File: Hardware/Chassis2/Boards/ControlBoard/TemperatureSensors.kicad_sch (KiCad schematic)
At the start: 4 parts, among them J5 TBP02R2W-381-08BE

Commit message: update hw revision 7
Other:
- company: (none) -> Corzine Lab, University of California, Santa Cruz
- title: (none) -> Open Inverter Platform - Control Board
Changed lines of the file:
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@@
 	(generator "eeschema")
 	(generator_version "10.0")
-	(paper "A4")
+	(paper "USLetter")
+	(title_block
+		(title "Open Inverter Platform - Control Board")
+		(date "2026-07-07")
+		(rev "G")
+		(company "Corzine Lab, University of California, Santa Cruz")
+		(comment 1 "Prepared by Thomas Liao")
+	)
 	(junction
 		(at 44.45 40.64)

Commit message: eod 2026-07-08
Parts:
- removed J5: TBP02R2W-381-08BE, TBP02R2W38108BE, symbol InverterCom:TBP02R2W-381-08BE
- removed R13, R29, R30: 10k, Resistor_SMD:R_1210_3225Metric_Pad1.30x2.65mm_HandSolder, symbol Device:R
- added C208, C209, C210, C211: 10uF, Capacitor_SMD:C_1210_3225Metric_Pad1.33x2.70mm_HandSolder, symbol Device:C
- added J1, J4, J5: B2B-XH-AM_LF__SN_, InverterCom:B2BXHAMLFSN, symbol InverterCom:B2B-XH-AM_LF__SN_
- added R90, R92, R94, R96: 10k, Resistor_SMD:R_1210_3225Metric_Pad1.30x2.65mm_HandSolder, symbol Device:R
- added R91, R93, R95, R97: 1k, Resistor_SMD:R_1210_3225Metric_Pad1.30x2.65mm_HandSolder, symbol Device:R
- added Z5, Z6, Z7, Z8: MM3Z3V0ST1G, InverterCom:SOD2512X100N, symbol InverterCom:MM3Z3V0ST1G
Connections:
- net +3.3V_V: now also R90.2, R92.2, R94.2, R96.2
- net GND_V: now also C208.2, C209.2, C210.2, C211.2, J1.1, J4.1, J5.1, Z5.2 (A), Z6.2 (A), Z7.2 (A), Z8.2 (A)
- net HEATSINK_TMP2_V: now also C209.1, R93.1
- net HEATSINK_TMP3_V: now also C210.1, R95.1
- net HEATSINK_TMP_V: now also C208.1, R91.1
- new net: J4.2, R92.1, R93.2, Z6.1 (K)
- new net: J5.2, R94.1, R95.2, Z7.1 (K)
- new net: J1.2, R90.1, R91.2, Z5.1 (K)
- new net MOTOR_TEMP_IN: R96.1, R97.2, Z8.1 (K)
- new net MOTOR_TEMP_V: C211.1, R97.1
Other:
- note added: "10K thermistor from motor if using different value thermistor, adjust resistor accordingly"
- note added: "10k THERMISTOR CONNECTOR"
- note added: "3v zener, clamps below 3.6v max input to STM32"
- note added: "For 10k NTC thermistor NOTE: Tempsense 1,2,3 are intended for monitoring IGBT module 1,2,3 system uses 2oo3 voting to exclude outlier temperature as unlikely HARA determines SSO/STO potentially more dangerous to use 1oo3 vs 2oo3"
- note added: "RC filter gives a bandwidth of ~16Hz HARA determines 16hz is acceptable. fc = 1/(2π × 1,000 Ω × 10 μF) = 15.915 Hz"
- note added: "tie other end of motor thermistor to gnd_v"

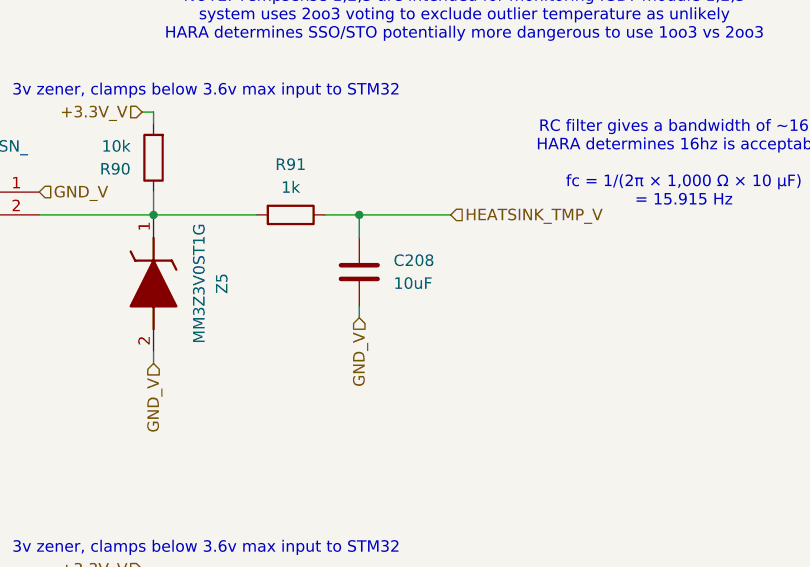
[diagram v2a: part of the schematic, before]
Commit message: Add Schematic / Controlboard Support for Multi-Drive Mulit-Phase, DDCP
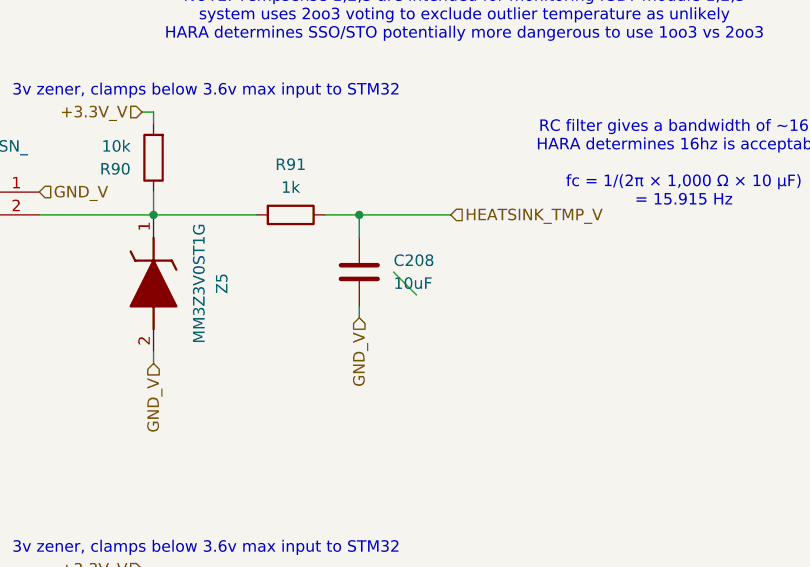
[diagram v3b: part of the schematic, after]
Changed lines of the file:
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@@
 		(color 0 0 0 0)
+	)
+	(bus_entry
+		(at 80.01 49.53)
+		(size 2.54 2.54)
+		(stroke
+			(width 0)
+			(type default)
+		)
 	)
 	(wire

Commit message: Labels tool, composite board views, InverterGen5 C2 branding, even render resolution
- Labels.pdf: HV warning labels, chassis ID, per-assembly labels (label cmd)
- Board sections add composite front/back views (PCB-viewer look, mirrored
  back) and layer plots now carry the drawing sheet with true plot scale
- Branding standardized to InverterGen5 C2 (cover, footer, labels)
- STEP previews render at even resolution regardless of part aspect
- Fab part titles from info.txt PartName; ALL-CAPS handling fixed
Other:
- title: Open Inverter Platform - Control Board -> InverterGen5 - Control Board
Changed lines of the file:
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@@
 	(paper "USLetter")
 	(title_block
-		(title "Open Inverter Platform - Control Board")
+		(title "InverterGen5 - Control Board")
 		(date "2026-07-07")
 		(rev "A")
